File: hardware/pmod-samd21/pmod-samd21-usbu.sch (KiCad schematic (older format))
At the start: 21 parts, among them J1 PMOD-2x6-MALE, J2 PMOD-2x6-FEMALE, J3 USB_C_Receptacle_USB2.0, Q1 2N7002PW, U1 ATSAMD21G-A, Y1 32.768kHz

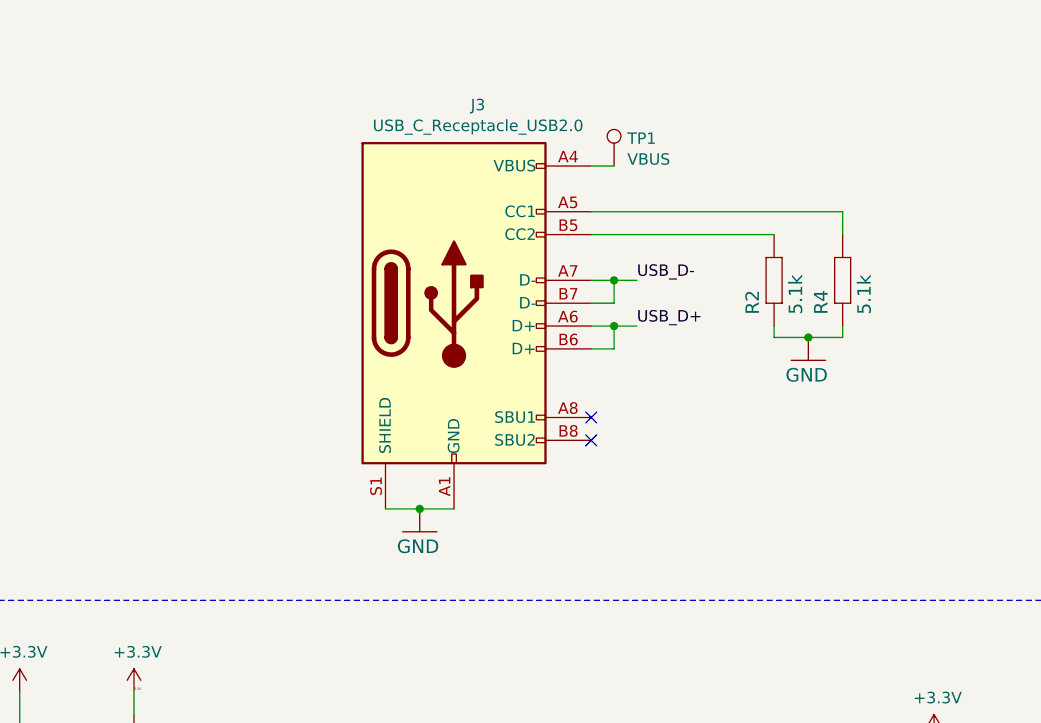
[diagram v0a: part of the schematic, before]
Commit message: SAMD21 PMOD microusb version
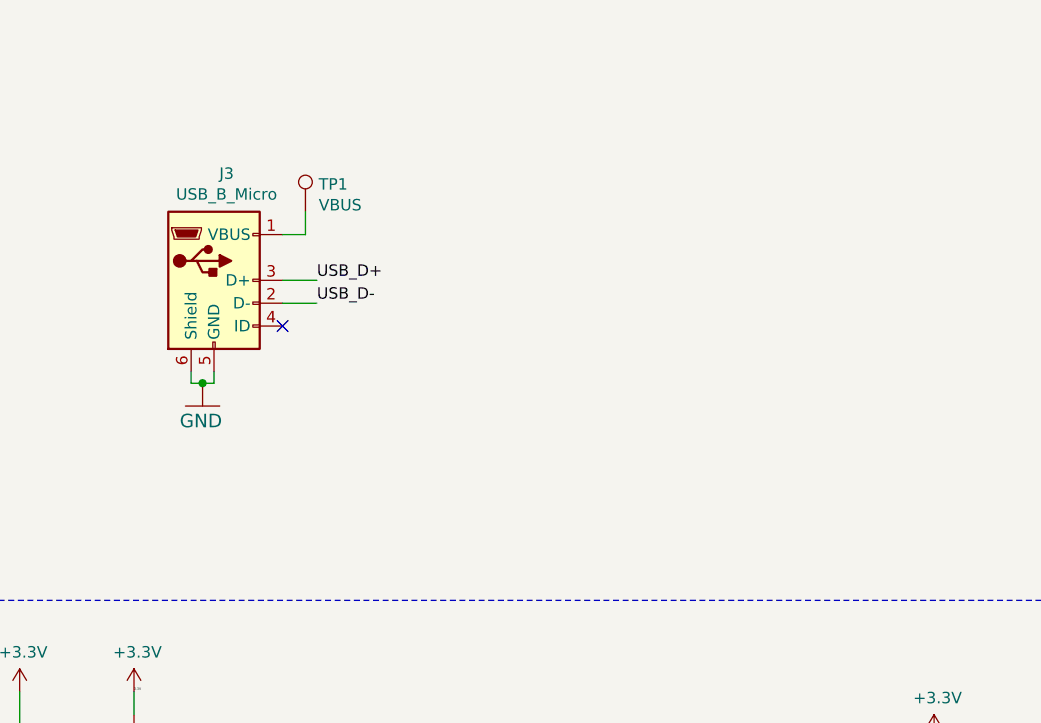
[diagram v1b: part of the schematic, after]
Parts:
- removed J3: USB_C_Receptacle_USB2.0, tom-connectors:USB_C_Receptacle_GT-USB-7010, symbol Connector:USB_C_Receptacle_USB2.0
- removed R2, R4: 5.1k, Resistors_SMD:R_0402, symbol pmod-samd21-eagle-import:R-EU_R0402
- added J3: USB_B_Micro, tom-connectors:USB_MICRO_TAOBAO_SMD_PTH, symbol Connector:USB_B_Micro
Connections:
- net USB_D+: now also J3.3 (D+)
- net USB_D-: now also J3.2 (D-)
- net VBUS: no longer names the net of TP1.1
- net VBUS: now also J3.1 (VBUS)
- new net: J3.5 (GND), J3.6 (Shield)
- no-connect marks 21 -> 20
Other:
- moved on the sheet: TP1
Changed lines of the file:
@@
 EESchema Schematic File Version 4
-LIBS:pmod-samd21-cache
 EELAYER 26 0
 EELAYER END
@@
 Wire Notes Line
 	900  3200 10700 3200
-$Comp
-L pmod-samd21-eagle-import:GND #GND08
-U 1 0 167E2C6ADF24F9E8
-P 3750 2900
-F 0 "#GND08" H 3750 2900 50  0001 C CNN
-F 1 "GND" H 3650 2800 59  0000 L BNN
-F 2 "" H 3750 2900 50  0001 C CNN
-F 3 "" H 3750 2900 50  0001 C CNN
-	1    3750 2900
-	1    0    0    -1
-$EndComp
 Wire Wire Line
 	1200 4900 1200 5100
@@
 	1    0    0    -1
 $EndComp
-Text Label 4700 1800 0    50   ~ 0
-USB_D-
-Text Label 4700 2000 0    50   ~ 0
-USB_D+
 $Comp
 L Connector:TestPoint TP1
 U 1 1 5BDFE875
-P 4600 1300
-F 0 "TP1" H 4658 1420 50  0000 L CNN
-F 1 "VBUS" H 4658 1329 50  0000 L CNN
-F 2 "Measurement_Points:Measurement_Point_Round-SMD-Pad_Small" H 4800 1300 50  0001 C CNN
-F 3 "~" H 4800 1300 50  0001 C CNN
-	1    4600 1300
+P 3250 1500
+F 0 "TP1" H 3308 1620 50  0000 L CNN
+F 1 "VBUS" H 3308 1529 50  0000 L CNN
+F 2 "Measurement_Points:Measurement_Point_Round-SMD-Pad_Small" H 3450 1500 50  0001 C CNN
+F 3 "~" H 3450 1500 50  0001 C CNN
+	1    3250 1500
 	1    0    0    -1
 $EndComp
@@
 $EndComp
 $Comp
-L Connector:USB_C_Receptacle_USB2.0 J3
-U 1 1 5BE0D9D2
-P 3900 1900
-F 0 "J3" H 4005 2767 50  0000 C CNN
-F 1 "USB_C_Receptacle_USB2.0" H 4005 2676 50  0000 C CNN
-F 2 "tom-connectors:USB_C_Receptacle_GT-USB-7010" H 4050 1900 50  0001 C CNN
-F 3 "https://www.usb.org/sites/default/files/documents/usb_type-c.zip" H 4050 1900 50  0001 C CNN
-	1    3900 1900
-	1    0    0    -1
-$EndComp
-Wire Wire Line
-	3900 2800 3750 2800
-Wire Wire Line
-	3750 2800 3600 2800
-Connection ~ 3750 2800
-Wire Wire Line
-	4600 1300 4500 1300
-Wire Wire Line
-	4500 1800 4600 1800
-Wire Wire Line
-	4600 1800 4600 1900
-Wire Wire Line
-	4600 1900 4500 1900
-Wire Wire Line
-	4500 2000 4600 2000
-Wire Wire Line
-	4600 2000 4600 2100
-Wire Wire Line
-	4600 2100 4500 2100
-Wire Wire Line
-	4600 2000 4700 2000
-Connection ~ 4600 2000
-Wire Wire Line
-	4600 1800 4700 1800
-Connection ~ 4600 1800
-$Comp
 L pmod-samd21-eagle-import:SWITCH-MOMENTARY-2SMD S1
 U 1 1 5BE31B43
@@
 Wire Wire Line
 	2100 6750 2100 7000
-NoConn ~ 4500 2500
-NoConn ~ 4500 2400
 $Comp
 L Device:Crystal Y1
@@
 	1900 5600 2500 5600
 $Comp
-L pmod-samd21-eagle-import:R-EU_R0402 R2
-U 1 0 5C0A44EE
-P 5300 1800
-F 0 "R2" H 5150 1859 59  0000 L BNN
-F 1 "5.1k" H 5150 1670 59  0000 L BNN
-F 2 "Resistors_SMD:R_0402" H 5300 1800 50  0001 C CNN
-F 3 "" H 5300 1800 50  0001 C CNN
-	1    5300 1800
-	0    -1   -1   0
-$EndComp
-$Comp
-L pmod-samd21-eagle-import:R-EU_R0402 R4
-U 1 0 5C0A4650
-P 5600 1800
-F 0 "R4" H 5450 1859 59  0000 L BNN
-F 1 "5.1k" H 5450 1670 59  0000 L BNN
-F 2 "Resistors_SMD:R_0402" H 5600 1800 50  0001 C CNN
-F 3 "" H 5600 1800 50  0001 C CNN
-	1    5600 1800
-	0    -1   -1   0
-$EndComp
+L Connector:USB_B_Micro J3
+U 1 1 5C0AD903
+P 2850 1800
+F 0 "J3" H 2905 2267 50  0000 C CNN
+F 1 "USB_B_Micro" H 2905 2176 50  0000 C CNN
+F 2 "tom-connectors:USB_MICRO_TAOBAO_SMD_PTH" H 3000 1750 50  0001 C CNN
+F 3 "~" H 3000 1750 50  0001 C CNN
+	1    2850 1800
+	1    0    0    -1
+$EndComp
+Wire Wire Line
+	3150 1800 3300 1800
+Wire Wire Line
+	3150 1900 3300 1900
+Text Label 3300 1800 0    50   ~ 0
+USB_D+
+Text Label 3300 1900 0    50   ~ 0
+USB_D-
 $Comp
 L pmod-samd21-eagle-import:GND #GND05
-U 1 0 5C0A4784
-P 5450 2150
-F 0 "#GND05" H 5450 2150 50  0001 C CNN
-F 1 "GND" H 5350 2050 59  0000 L BNN
-F 2 "" H 5450 2150 50  0001 C CNN
-F 3 "" H 5450 2150 50  0001 C CNN
-	1    5450 2150
-	1    0    0    -1
-$EndComp
-Wire Wire Line
-	5300 2000 5300 2050
-Wire Wire Line
-	5300 2050 5450 2050
-Wire Wire Line
-	5450 2050 5600 2050
-Wire Wire Line
-	5600 2050 5600 2000
-Connection ~ 5450 2050
-Wire Wire Line
-	5300 1600 4500 1600
-Wire Wire Line
-	4500 1500 5600 1500
-Wire Wire Line
-	5600 1500 5600 1600
+U 1 0 5C0B8765
+P 2800 2350
+F 0 "#GND05" H 2800 2350 50  0001 C CNN
+F 1 "GND" H 2700 2250 59  0000 L BNN
+F 2 "" H 2800 2350 50  0001 C CNN
+F 3 "" H 2800 2350 50  0001 C CNN
+	1    2800 2350
+	1    0    0    -1
+$EndComp
+Wire Wire Line
+	3150 1600 3250 1600
+Wire Wire Line
+	3250 1600 3250 1500
+Wire Wire Line
+	2750 2200 2750 2250
+Wire Wire Line
+	2750 2250 2800 2250
+Wire Wire Line
+	2850 2200 2850 2250
+Wire Wire Line
+	2850 2250 2800 2250
+Connection ~ 2800 2250
+NoConn ~ 3150 2000
 $EndSCHEMATC

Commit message: pmod-samd21 : changes for seeed studio opl fabrication
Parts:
- C1, C2, C3, C4: SKU (none) -> 0402B104K160CT
- C5, C6: value 15pF -> 6pF; SKU (none) -> 0402CG6R0C500NT
- C7: renamed from C9; value 0.1uF -> 1uF; SKU (none) -> CC0402KRX5R5BB105
- D1: SKU (none) -> 16-213/BHC-AN1P2/3T
- J1, J2, TP1: SKU (none) -> DO_NOT_POPULATE
- J3: SKU (none) -> U-F-M5DD-Y-1
- J4: renamed from JP2; SKU (none) -> DO_NOT_POPULATE
- Q1: SKU (none) -> 2N7002,215
- R1: SKU (none) -> RC0402JR-0710KL
- R2: renamed from R3; SKU (none) -> RC0402FR-07330RL
- S1: SKU (none) -> K2-1101ST-A4SA-01
- U1: SKU (none) -> ATSAMD21G18A-AU
- Y1: SKU (none) -> Q13FC1350004900
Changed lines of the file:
@@
 EESchema Schematic File Version 4
+LIBS:pmod-samd21-usbu-cache
 EELAYER 26 0
 EELAYER END
@@
 F 2 "tom-semiconductors:QFP50P900X900X120-48N" H 3950 5900 50  0001 C CNN
 F 3 "" H 3950 5900 50  0001 C CNN
+F 4 "ATSAMD21G18A-AU" H 3950 5900 50  0001 C CNN "SKU"
 	1    3950 5900
 	1    0    0    -1
@@
 F 2 "Capacitors_SMD:C_0402" H 2000 4600 50  0001 C CNN
 F 3 "" H 2000 4600 50  0001 C CNN
+F 4 "0402B104K160CT" H 2000 4600 50  0001 C CNN "SKU"
 	1    2000 4600
 	-1   0    0    -1
@@
 F 2 "Capacitors_SMD:C_0402" H 2500 4650 50  0001 C CNN
 F 3 "" H 2500 4650 50  0001 C CNN
+F 4 "0402B104K160CT" H 2500 4650 50  0001 C CNN "SKU"
 	1    2500 4650
 	-1   0    0    -1
@@
 F 2 "Capacitors_SMD:C_0402" H 1200 5400 50  0001 C CNN
 F 3 "" H 1200 5400 50  0001 C CNN
+F 4 "0402B104K160CT" H 1200 5400 50  0001 C CNN "SKU"
 	1    1200 5400
 	-1   0    0    -1
@@
 F 2 "Capacitors_SMD:C_0402" H 6000 4400 50  0001 C CNN
 F 3 "" H 6000 4400 50  0001 C CNN
+F 4 "0402B104K160CT" H 6000 4400 50  0001 C CNN "SKU"
 	1    6000 4400
 	1    0    0    -1
@@
 F 2 "Resistors_SMD:R_0402" H 2500 3900 50  0001 C CNN
 F 3 "" H 2500 3900 50  0001 C CNN
+F 4 "RC0402JR-0710KL" H 2500 3900 50  0001 C CNN "SKU"
 	1    2500 3900
 	0    -1   -1   0
@@
 P 1650 5300
 F 0 "C5" V 1635 5380 59  0000 L BNN
-F 1 "15pF" V 1665 5380 59  0000 L TNN
+F 1 "6pF" V 1665 5380 59  0000 L TNN
 F 2 "Capacitors_SMD:C_0402" H 1650 5300 50  0001 C CNN
 F 3 "" H 1650 5300 50  0001 C CNN
+F 4 "0402CG6R0C500NT" V 1650 5300 50  0001 C CNN "SKU"
 	1    1650 5300
 	0    -1   -1   0
@@
 P 1550 5600
 F 0 "C6" V 1535 5620 59  0000 R BNN
-F 1 "15pF" V 1565 5690 59  0000 L TNN
+F 1 "6pF" V 1565 5690 59  0000 L TNN
 F 2 "Capacitors_SMD:C_0402" H 1550 5600 50  0001 C CNN
 F 3 "" H 1550 5600 50  0001 C CNN
+F 4 "0402CG6R0C500NT" V 1550 5600 50  0001 C CNN "SKU"
 	1    1550 5600
 	0    1    1    0
@@
 $EndComp
 $Comp
-L pmod-samd21-eagle-import:R-EU_R0402 R3
+L pmod-samd21-eagle-import:R-EU_R0402 R2
 U 1 0 C7959A8847515AA7
 P 7200 1600
-F 0 "R3" H 7050 1659 59  0000 L BNN
+F 0 "R2" H 7050 1659 59  0000 L BNN
 F 1 "330" H 7050 1470 59  0000 L BNN
 F 2 "Resistors_SMD:R_0402" H 7200 1600 50  0001 C CNN
 F 3 "" H 7200 1600 50  0001 C CNN
+F 4 "RC0402FR-07330RL" H 7200 1600 50  0001 C CNN "SKU"
 	1    7200 1600
 	0    -1   -1   0
@@
 F 2 "TO_SOT_Packages_SMD:SOT-323_SC-70_Handsoldering" H 7200 2500 50  0001 C CNN
 F 3 "" H 7200 2500 50  0001 C CNN
+F 4 "2N7002,215" H 7200 2500 50  0001 C CNN "SKU"
 	1    7200 2500
 	-1   0    0    -1
 $EndComp
 $Comp
-L pmod-samd21-eagle-import:CORTEX_DEBUGPTH JP2
+L pmod-samd21-eagle-import:CORTEX_DEBUGPTH J4
 U 1 0 F946090C8F370CD1
 P 8700 4000
-F 0 "JP2" H 8200 4310 59  0000 L BNN
+F 0 "J4" H 8200 4310 59  0000 L BNN
 F 1 "CORTEX_DEBUGPTH" H 8200 3690 59  0000 L TNN
 F 2 "tom-connectors:CONN_1.27_2x5" H 8700 4000 50  0001 C CNN
 F 3 "" H 8700 4000 50  0001 C CNN
+F 4 "DO_NOT_POPULATE" H 8700 4000 50  0001 C CNN "SKU"
 	1    8700 4000
 	1    0    0    -1
@@
 $EndComp
 $Comp
-L pmod-samd21-eagle-import:0.1UF-16V(+-10%)(0402) C9
+L pmod-samd21-eagle-import:0.1UF-16V(+-10%)(0402) C7
 U 1 0 8514EC1FF7AEDC46
 P 6400 4400
-F 0 "C9" H 6460 4515 59  0000 L BNN
-F 1 "0.1uF" H 6460 4315 59  0000 L BNN
+F 0 "C7" H 6460 4515 59  0000 L BNN
+F 1 "1uF" H 6460 4315 59  0000 L BNN
 F 2 "Capacitors_SMD:C_0402" H 6400 4400 50  0001 C CNN
 F 3 "" H 6400 4400 50  0001 C CNN
+F 4 "CC0402KRX5R5BB105" H 6400 4400 50  0001 C CNN "SKU"
 	1    6400 4400
 	1    0    0    -1
@@
 F 2 "tom-connectors:2X6_SMD_RA_PLUG" H 7750 5500 50  0001 C CNN
 F 3 "" H 7750 5500 50  0001 C CNN
+F 4 "DO_NOT_POPULATE" H 7750 5500 50  0001 C CNN "SKU"
 	1    7750 5500
 	1    0    0    -1
@@
 F 2 "tom-connectors:2X6_SMD_RA_SOCKET" H 9650 5600 50  0001 C CNN
 F 3 "" H 9650 5600 50  0001 C CNN
+F 4 "DO_NOT_POPULATE" H 9650 5600 50  0001 C CNN "SKU"
 	1    9650 5600
 	1    0    0    -1
@@
 F 2 "Measurement_Points:Measurement_Point_Round-SMD-Pad_Small" H 3450 1500 50  0001 C CNN
 F 3 "~" H 3450 1500 50  0001 C CNN
+F 4 "DO_NOT_POPULATE" H 3250 1500 50  0001 C CNN "SKU"
 	1    3250 1500
 	1    0    0    -1
@@
 F 2 "LEDs:LED_0402" H 7200 2050 50  0001 C CNN
 F 3 "~" H 7200 2050 50  0001 C CNN
+F 4 "16-213/BHC-AN1P2/3T" V 7200 2050 50  0001 C CNN "SKU"
 	1    7200 2050
 	0    -1   -1   0
@@
 F 2 "tom-mechanical:SW_SPST_SMD_2PIN_3.5x6.0" H 1800 6750 50  0001 C CNN
 F 3 "" H 1800 6750 50  0001 C CNN
+F 4 "K2-1101ST-A4SA-01" H 1800 6750 50  0001 C CNN "SKU"
 	1    1800 6750
 	1    0    0    -1
@@
 F 2 "Crystals:Crystal_SMD_3215-2pin_3.2x1.5mm" H 1900 5450 50  0001 C CNN
 F 3 "~" H 1900 5450 50  0001 C CNN
+F 4 "Q13FC1350004900" V 1900 5450 50  0001 C CNN "SKU"
 	1    1900 5450
 	0    -1   -1   0
@@
 F 2 "tom-connectors:USB_MICRO_TAOBAO_SMD_PTH" H 3000 1750 50  0001 C CNN
 F 3 "~" H 3000 1750 50  0001 C CNN
+F 4 "U-F-M5DD-Y-1" H 2850 1800 50  0001 C CNN "SKU"
 	1    2850 1800
 	1    0    0    -1

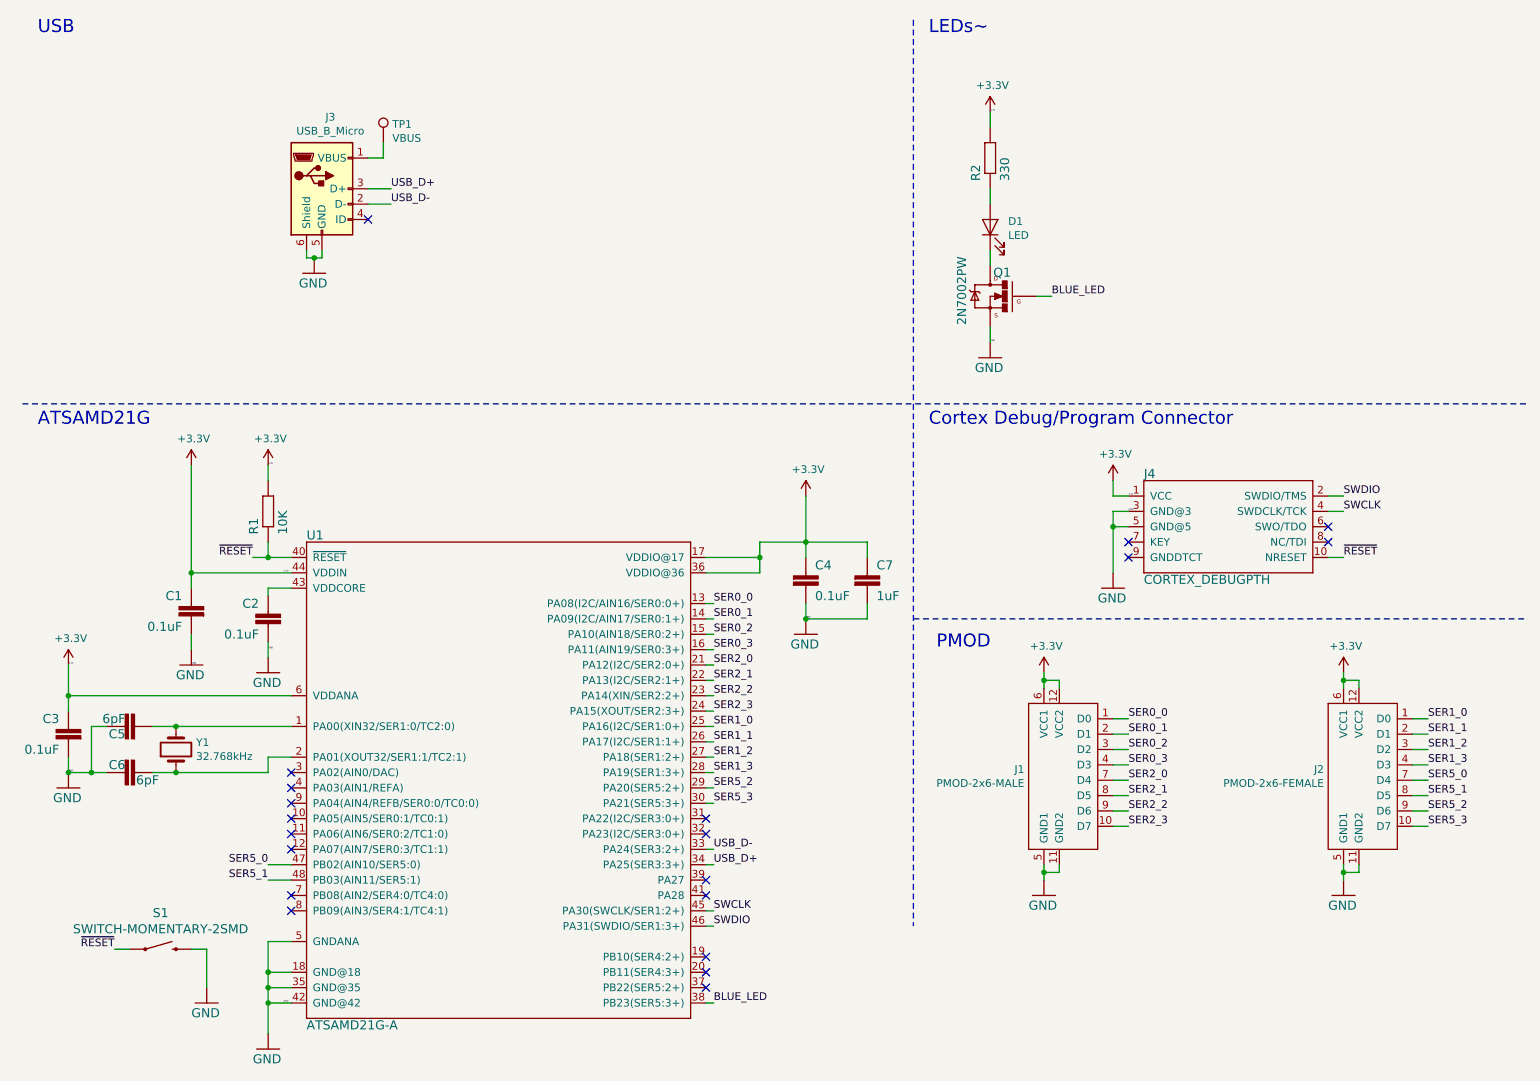
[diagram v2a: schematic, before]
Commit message: Fix IO assignments on PMOD so both i2c and spi work
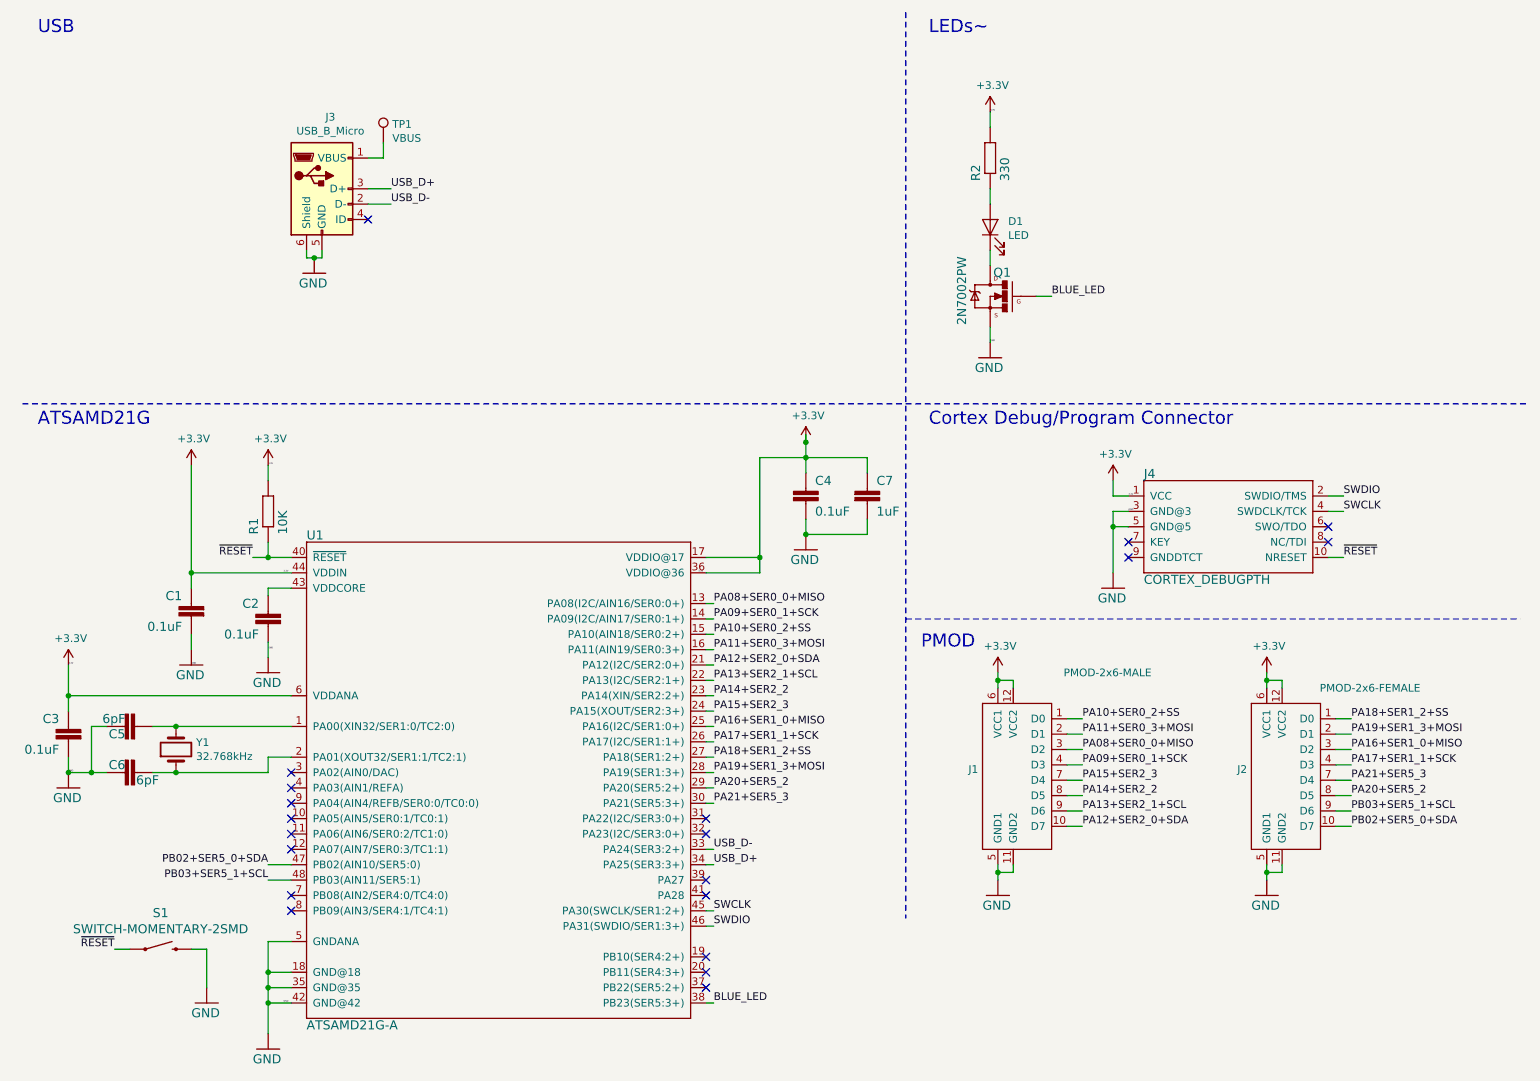
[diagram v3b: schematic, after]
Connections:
- net GND: no longer C4.2, C7.2
- net SER0_0 renamed PA08+SER0_0+MISO
- net PA08+SER0_0+MISO: now also J1.3 (D2); no longer J1.1 (D0)
- net SER0_1 renamed PA09+SER0_1+SCK
- net PA09+SER0_1+SCK: now also J1.4 (D3); no longer J1.2 (D1)
- net SER0_2 renamed PA10+SER0_2+SS
- net PA10+SER0_2+SS: now also J1.1 (D0); no longer J1.3 (D2)
- net SER0_3 renamed PA11+SER0_3+MOSI
- net PA11+SER0_3+MOSI: now also J1.2 (D1); no longer J1.4 (D3)
- net SER1_0 renamed PA16+SER1_0+MISO
- net PA16+SER1_0+MISO: now also J2.3 (D2); no longer J2.1 (D0)
- net SER1_1 renamed PA17+SER1_1+SCK
- net PA17+SER1_1+SCK: now also J2.4 (D3); no longer J2.2 (D1)
- net SER1_2 renamed PA18+SER1_2+SS
- net PA18+SER1_2+SS: now also J2.1 (D0); no longer J2.3 (D2)
- net SER1_3 renamed PA19+SER1_3+MOSI
- net PA19+SER1_3+MOSI: now also J2.2 (D1); no longer J2.4 (D3)
- net SER2_0 renamed PA12+SER2_0+SDA
- net PA12+SER2_0+SDA: now also J1.10 (D7); no longer J1.7 (D4)
- net SER2_1 renamed PA13+SER2_1+SCL
- net PA13+SER2_1+SCL: now also J1.9 (D6); no longer J1.8 (D5)
- net SER2_2 renamed PA14+SER2_2
- net PA14+SER2_2: now also J1.8 (D5); no longer J1.9 (D6)
- net SER2_3 renamed PA15+SER2_3
- net PA15+SER2_3: now also J1.7 (D4); no longer J1.10 (D7)
- net SER5_0 renamed PA21+SER5_3
- net PA21+SER5_3: now also U1.30 (PA21(SER5:3+)); no longer U1.47 (PB02(AIN10/SER5:0))
- net SER5_1 renamed PA20+SER5_2
- net PA20+SER5_2: now also U1.29 (PA20(SER5:2+)); no longer U1.48 (PB03(AIN11/SER5:1))
- net SER5_2 renamed PB03+SER5_1+SCL
- net PB03+SER5_1+SCL: now also U1.48 (PB03(AIN11/SER5:1)); no longer U1.29 (PA20(SER5:2+))
- net SER5_3 renamed PB02+SER5_0+SDA
- net PB02+SER5_0+SDA: now also U1.47 (PB02(AIN10/SER5:0)); no longer U1.30 (PA21(SER5:3+))
- new net: C4.2, C7.2
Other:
- moved on the sheet: J1, J2
